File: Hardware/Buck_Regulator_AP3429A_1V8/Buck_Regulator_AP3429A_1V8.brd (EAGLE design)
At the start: 25.4 x 25.4 mm, 51 parts, among them J1 Screw Terminal, J2 POWER_JACKPOWER_JACK_SLOT_COM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, J3 Breakout Headers, U1 AP3429/A

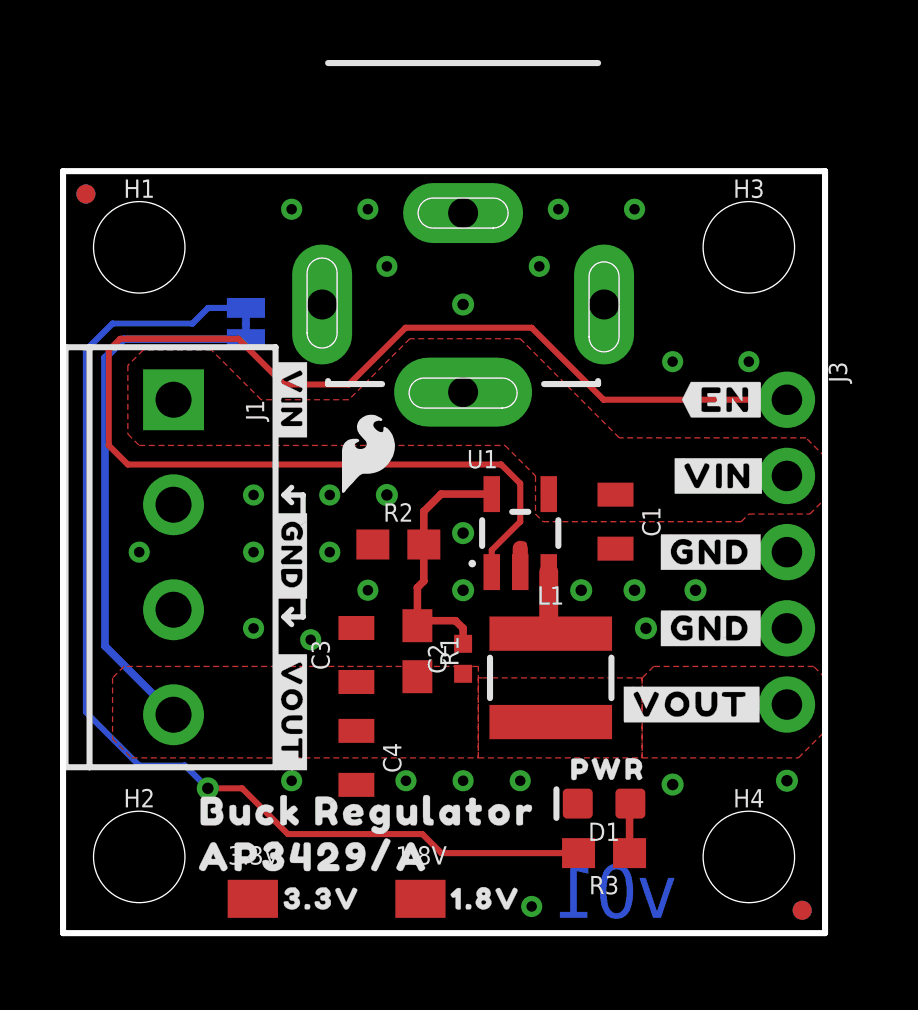
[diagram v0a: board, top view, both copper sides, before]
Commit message: Nudge traces for better GND pour connection on BRD
Moved some traces for a better GND pour on the top layer.
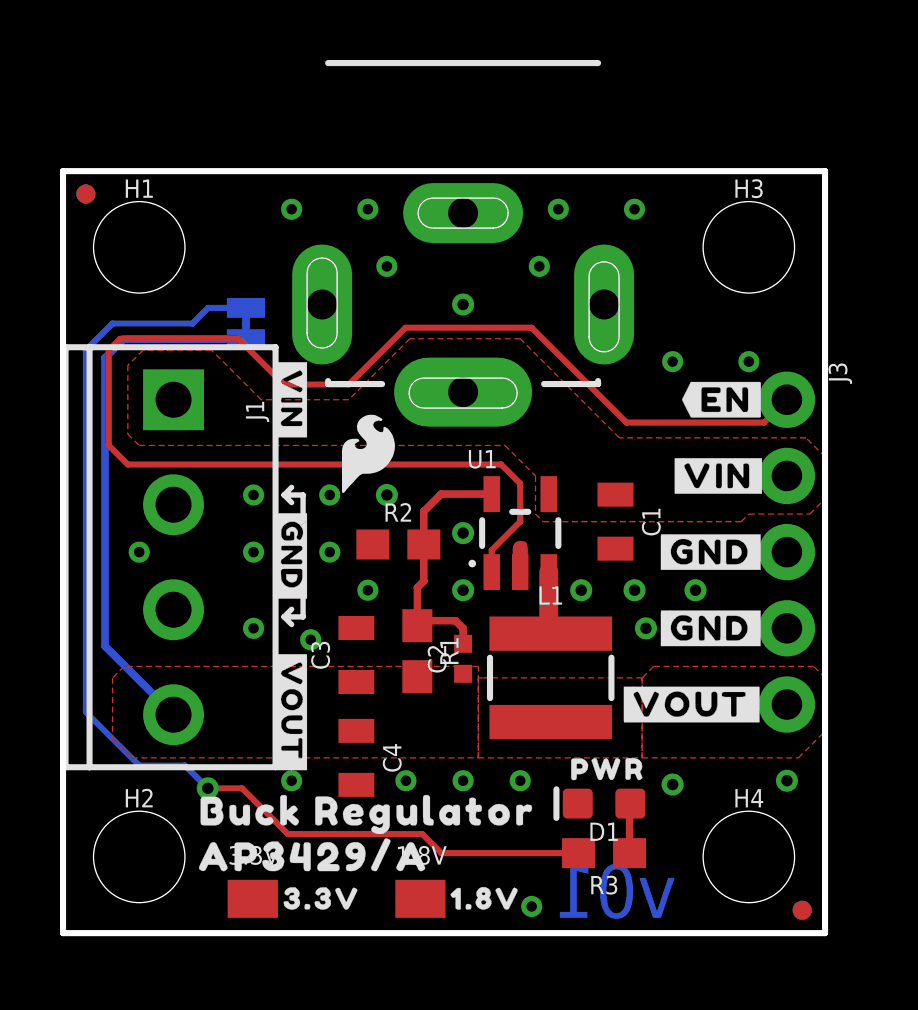
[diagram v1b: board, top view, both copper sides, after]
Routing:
- net EN: track 45.9 -> 46.6 mm
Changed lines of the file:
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@@
 <wire x1="1.524" y1="16.256" x2="1.524" y2="19.431" width="0.2032" layer="1"/>
 <wire x1="1.524" y1="19.431" x2="1.905" y2="19.812" width="0.2032" layer="1"/>
-<wire x1="15.61835" y1="20.1803" x2="18.01865" y2="17.78" width="0.2032" layer="1"/>
+<wire x1="15.61835" y1="20.1803" x2="18.78065" y2="17.018" width="0.2032" layer="1"/>
 <wire x1="1.905" y1="19.812" x2="5.842" y2="19.812" width="0.2032" layer="1"/>
 <wire x1="5.842" y1="19.812" x2="7.366" y2="18.288" width="0.2032" layer="1"/>
@@
 <wire x1="9.525" y1="18.288" x2="11.4173" y2="20.1803" width="0.2032" layer="1"/>
 <wire x1="11.4173" y1="20.1803" x2="15.61835" y2="20.1803" width="0.2032" layer="1"/>
-<wire x1="24.13" y1="17.78" x2="18.01865" y2="17.78" width="0.2032" layer="1"/>
+<wire x1="24.13" y1="17.78" x2="23.368" y2="17.018" width="0.2032" layer="1"/>
+<wire x1="23.368" y1="17.018" x2="18.78065" y2="17.018" width="0.2032" layer="1"/>
 </signal>
 <signal name="N$3">

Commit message: Added correct measurements
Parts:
- moved FRAME1 24.1 mm to (-10.2, -41.9)
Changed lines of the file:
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@@
 <drawing>
 <settings>
-<setting alwaysvectorfont="yes"/>
+<setting alwaysvectorfont="no"/>
 <setting verticaltext="up"/>
 </settings>
@@
 <layer number="45" name="Holes" color="7" fill="1" visible="yes" active="yes"/>
 <layer number="46" name="Milling" color="3" fill="1" visible="no" active="yes"/>
-<layer number="47" name="Measures" color="7" fill="1" visible="no" active="yes"/>
+<layer number="47" name="Measures" color="7" fill="1" visible="yes" active="yes"/>
 <layer number="48" name="Document" color="7" fill="1" visible="no" active="yes"/>
 <layer number="49" name="Reference" color="7" fill="1" visible="no" active="yes"/>
@@
 <wire x1="7.366" y1="10.541" x2="7.62" y2="10.287" width="0.1778" layer="21"/>
 <text x="20.447" y="0.508" size="1.778" layer="16" font="vector" ratio="15" rot="MR0">v01</text>
-<text x="16.51" y="-17.78" size="1.778" layer="51" font="vector" ratio="10" distance="15">M. Chodikov</text>
-<text x="5.08" y="46.99" size="1.778" layer="47" font="vector" ratio="15">Units in Inches</text>
+<text x="16.51" y="-41.91" size="1.778" layer="51" font="vector" ratio="10" distance="15">M. Chodikov</text>
 <wire x1="5.334" y1="11.176" x2="5.334" y2="10.414" width="0.2032" layer="22"/>
 <wire x1="5.334" y1="10.414" x2="4.826" y2="10.414" width="0.2032" layer="22"/>
@@
 <rectangle x1="6.35" y1="3.81" x2="21.59" y2="16.51" layer="30" rot="R180"/>
 <wire x1="5.08" y1="11.43" x2="5.334" y2="11.176" width="0.2032" layer="22"/>
-<dimension x1="25.4" y1="25.4" x2="22.86" y2="25.4" x3="24.13" y3="29.21" textsize="1.778" textratio="15" layer="47" unit="inch"/>
-<dimension x1="2.54" y1="22.86" x2="0" y2="22.86" x3="1.27" y3="35.56" textsize="1.778" textratio="15" layer="47" unit="inch"/>
-<dimension x1="25.4" y1="25.4" x2="0" y2="25.4" x3="12.7" y3="40.64" textsize="1.778" textratio="15" layer="47" unit="inch"/>
-<dimension x1="2.54" y1="2.54" x2="2.54" y2="0" x3="-2.54" y3="1.27" textsize="1.778" textratio="15" layer="47" unit="inch"/>
-<dimension x1="2.54" y1="22.86" x2="2.54" y2="25.4" x3="-2.54" y3="24.13" textsize="1.778" textratio="15" layer="47" unit="inch"/>
-<dimension x1="3.683" y1="7.28" x2="3.81" y2="0" x3="-8.89" y3="3.64" textsize="1.778" textratio="15" layer="47" dtype="vertical" unit="inch"/>
-<dimension x1="3.683" y1="7.28" x2="3.81" y2="10.795" x3="-13.97" y3="9.0375" textsize="1.778" textratio="15" layer="47" dtype="vertical" unit="inch"/>
-<dimension x1="0" y1="25.4" x2="0" y2="0" x3="-20.32" y3="12.7" textsize="1.778" textratio="15" layer="47" unit="inch"/>
-<dimension x1="24.13" y1="7.493" x2="24.13" y2="0" x3="30.48" y3="3.7465" textsize="1.778" textratio="15" layer="47" unit="inch"/>
-<dimension x1="24.13" y1="7.62" x2="24.13" y2="10.16" x3="30.48" y3="8.89" textsize="1.778" textratio="15" layer="47" unit="inch"/>
+<dimension x1="2.54" y1="2.54" x2="0" y2="2.54" x3="1.27" y3="-3.81" textsize="1.778" layer="47" unit="inch"/>
+<dimension x1="3.683" y1="7.28" x2="3.683" y2="0" x3="-3.81" y3="3.64" textsize="1.778" layer="47" dtype="vertical" unit="inch"/>
+<dimension x1="24.13" y1="7.62" x2="24.13" y2="0" x3="-7.62" y3="3.81" textsize="1.778" layer="47" dtype="vertical" unit="inch"/>
+<dimension x1="24.13" y1="10.16" x2="24.13" y2="0" x3="-12.7" y3="5.08" textsize="1.778" layer="47" dtype="vertical" unit="inch"/>
+<dimension x1="3.683" y1="10.795" x2="3.937" y2="0" x3="-17.78" y3="5.3975" textsize="1.778" layer="47" dtype="vertical" unit="inch"/>
+<text x="-22.86" y="-10.16" size="1.778" layer="47" font="vector" ratio="15">Units in Inches</text>
+<dimension x1="2.54" y1="2.54" x2="2.54" y2="0" x3="-21.59" y3="1.27" textsize="1.778" layer="47" dtype="vertical" unit="inch"/>
+<dimension x1="2.54" y1="22.86" x2="2.54" y2="0" x3="-25.4" y3="11.43" textsize="1.778" layer="47" dtype="vertical" unit="inch"/>
+<dimension x1="13.335" y1="24.003" x2="13.97" y2="0" x3="-29.21" y3="12.0015" textsize="1.778" layer="47" dtype="vertical" unit="inch"/>
+<dimension x1="0" y1="0" x2="2.54" y2="25.4" x3="-33.02" y3="12.7" textsize="1.778" layer="47" dtype="vertical" unit="inch"/>
+<dimension x1="3.683" y1="17.78" x2="0" y2="17.78" x3="1.8415" y3="-7.62" textsize="1.778" layer="47" dtype="vertical" unit="inch"/>
+<dimension x1="13.335" y1="24.003" x2="0" y2="24.003" x3="6.6675" y3="-12.7" textsize="1.778" layer="47" dtype="vertical" unit="inch"/>
+<dimension x1="22.86" y1="2.54" x2="0" y2="2.54" x3="11.43" y3="-17.78" textsize="1.778" layer="47" dtype="vertical" unit="inch"/>
+<dimension x1="24.13" y1="7.62" x2="0" y2="7.62" x3="12.065" y3="-22.86" textsize="1.778" layer="47" dtype="vertical" unit="inch"/>
+<dimension x1="25.4" y1="0" x2="0" y2="0" x3="12.7" y3="-27.94" textsize="1.778" layer="47" dtype="vertical" unit="inch"/>
 </plain>
 <attributes>
@@
 <element name="FD3" library="SparkFun-Aesthetics" package="FIDUCIAL-MICRO" value="FIDUCIALUFIDUCIAL" x="0.762" y="24.638" smashed="yes" rot="MR0"/>
 <element name="FD4" library="SparkFun-Aesthetics" package="FIDUCIAL-MICRO" value="FIDUCIALUFIDUCIAL" x="0.762" y="24.638" smashed="yes"/>
-<element name="FRAME1" library="SparkFun-Aesthetics" package="CREATIVE_COMMONS" value="FRAME-LEDGER" x="-10.16" y="-17.78" smashed="yes">
-<attribute name="DESIGNER" value="M. Chodikov" x="69.85" y="-30.48" size="1.778" layer="27" display="off"/>
-<attribute name="REV" value="v01" x="69.85" y="-30.48" size="1.778" layer="27" display="off"/>
+<element name="FRAME1" library="SparkFun-Aesthetics" package="CREATIVE_COMMONS" value="FRAME-LEDGER" x="-10.16" y="-41.91" smashed="yes">
+<attribute name="DESIGNER" value="M. Chodikov" x="69.85" y="-54.61" size="1.778" layer="27" display="off"/>
+<attribute name="REV" value="v01" x="69.85" y="-54.61" size="1.778" layer="27" display="off"/>
 </element>
 <element name="L1" library="SparkFun-Coils" package="INDUCTOR_4X4MM" value="2.2μH" x="16.256" y="8.509" smashed="yes">

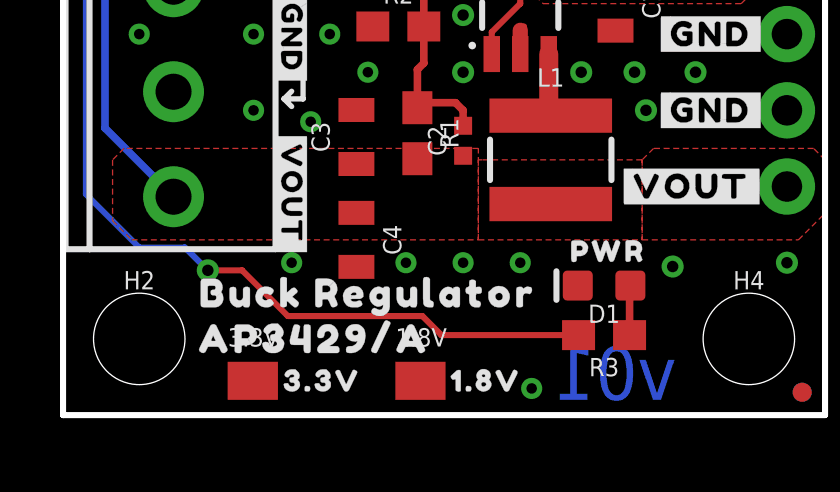
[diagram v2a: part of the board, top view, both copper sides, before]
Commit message: Further design review changes - v01
Added selective solder path to Document layer for the terminal block; moved the silkscreen name on the front to not be covered by the mounting hole anymore when a user uses a screw; nudges the LED power trace over for better GND connection; added measures to thermal pad (in reference to bottom right, and for the size)
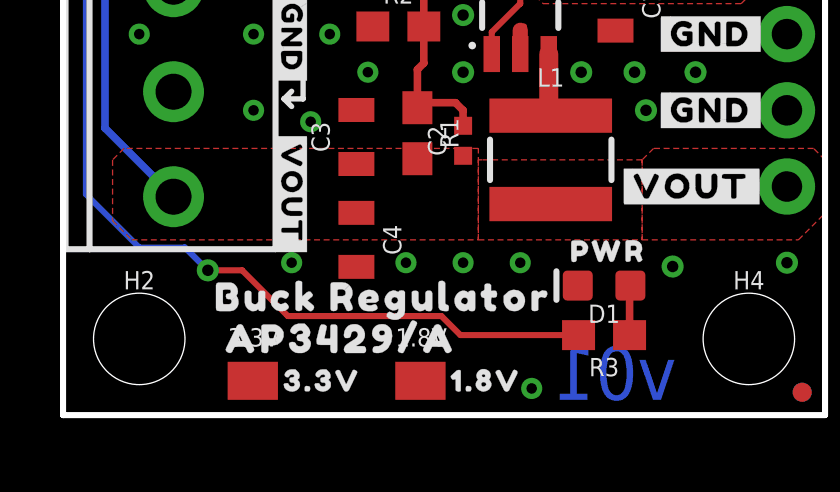
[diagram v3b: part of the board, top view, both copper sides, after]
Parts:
- moved FRAME1 2.54 mm to (-10.2, -44.5)
- moved U$3 0.89 mm to (9.27, 2.54)
- moved U$2 0.52 mm to (10.7, 3.94)
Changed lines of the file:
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@@
 <layer number="28" name="bValues" color="7" fill="1" visible="no" active="yes"/>
 <layer number="29" name="tStop" color="7" fill="3" visible="no" active="yes"/>
-<layer number="30" name="bStop" color="7" fill="6" visible="no" active="yes"/>
+<layer number="30" name="bStop" color="7" fill="6" visible="yes" active="yes"/>
 <layer number="31" name="tCream" color="7" fill="4" visible="no" active="yes"/>
 <layer number="32" name="bCream" color="7" fill="5" visible="no" active="yes"/>
@@
 <wire x1="7.366" y1="10.541" x2="7.62" y2="10.287" width="0.1778" layer="21"/>
 <text x="20.447" y="0.508" size="1.778" layer="16" font="vector" ratio="15" rot="MR0">v01</text>
-<text x="16.51" y="-41.91" size="1.778" layer="51" font="vector" ratio="10" distance="15">M. Chodikov</text>
+<text x="16.51" y="-44.45" size="1.778" layer="51" font="vector" ratio="10" distance="15">M. Chodikov</text>
 <wire x1="5.334" y1="11.176" x2="5.334" y2="10.414" width="0.2032" layer="22"/>
 <wire x1="5.334" y1="10.414" x2="4.826" y2="10.414" width="0.2032" layer="22"/>
@@
 <dimension x1="3.683" y1="10.795" x2="3.937" y2="0" x3="-17.78" y3="5.3975" textsize="1.778" layer="47" dtype="vertical" unit="inch"/>
 <text x="-22.86" y="-10.16" size="1.778" layer="47" font="vector" ratio="15">Units in Inches</text>
-<dimension x1="2.54" y1="2.54" x2="2.54" y2="0" x3="-21.59" y3="1.27" textsize="1.778" layer="47" dtype="vertical" unit="inch"/>
-<dimension x1="2.54" y1="22.86" x2="2.54" y2="0" x3="-25.4" y3="11.43" textsize="1.778" layer="47" dtype="vertical" unit="inch"/>
-<dimension x1="13.335" y1="24.003" x2="13.97" y2="0" x3="-29.21" y3="12.0015" textsize="1.778" layer="47" dtype="vertical" unit="inch"/>
-<dimension x1="0" y1="0" x2="2.54" y2="25.4" x3="-33.02" y3="12.7" textsize="1.778" layer="47" dtype="vertical" unit="inch"/>
 <dimension x1="3.683" y1="17.78" x2="0" y2="17.78" x3="1.8415" y3="-7.62" textsize="1.778" layer="47" dtype="vertical" unit="inch"/>
-<dimension x1="13.335" y1="24.003" x2="0" y2="24.003" x3="6.6675" y3="-12.7" textsize="1.778" layer="47" dtype="vertical" unit="inch"/>
-<dimension x1="22.86" y1="2.54" x2="0" y2="2.54" x3="11.43" y3="-17.78" textsize="1.778" layer="47" dtype="vertical" unit="inch"/>
-<dimension x1="24.13" y1="7.62" x2="0" y2="7.62" x3="12.065" y3="-22.86" textsize="1.778" layer="47" dtype="vertical" unit="inch"/>
-<dimension x1="25.4" y1="0" x2="0" y2="0" x3="12.7" y3="-27.94" textsize="1.778" layer="47" dtype="vertical" unit="inch"/>
+<wire x1="3.048" y1="16.891" x2="3.048" y2="6.35" width="5.9944" layer="48"/>
+<wire x1="3.048" y1="6.35" x2="0" y2="3.302" width="5.9944" layer="48"/>
+<dimension x1="6.35" y1="3.81" x2="0" y2="3.81" x3="3.175" y3="-12.7" textsize="1.778" textratio="15" layer="47" unit="inch"/>
+<dimension x1="13.335" y1="24.003" x2="0" y2="24.003" x3="6.6675" y3="-19.05" textsize="1.778" textratio="15" layer="47" unit="inch"/>
+<dimension x1="22.86" y1="2.54" x2="0" y2="2.54" x3="11.43" y3="-24.13" textsize="1.778" textratio="15" layer="47" unit="inch"/>
+<dimension x1="24.13" y1="7.62" x2="0" y2="7.62" x3="12.065" y3="-29.21" textsize="1.778" textratio="15" layer="47" unit="inch"/>
+<dimension x1="25.4" y1="0" x2="0" y2="0" x3="12.7" y3="-33.02" textsize="1.778" textratio="15" layer="47" unit="inch"/>
+<dimension x1="6.35" y1="3.81" x2="6.35" y2="0" x3="-21.59" y3="1.905" textsize="1.778" textratio="15" layer="47" unit="inch"/>
+<dimension x1="2.54" y1="2.54" x2="2.54" y2="0" x3="-25.4" y3="1.27" textsize="1.778" textratio="15" layer="47" unit="inch"/>
+<dimension x1="2.54" y1="22.86" x2="2.54" y2="0" x3="-29.21" y3="11.43" textsize="1.778" textratio="15" layer="47" unit="inch"/>
+<dimension x1="13.335" y1="24.003" x2="13.335" y2="0" x3="-33.02" y3="12.0015" textsize="1.778" textratio="15" layer="47" unit="inch"/>
+<dimension x1="0" y1="0" x2="0" y2="25.4" x3="-36.83" y3="12.7" textsize="1.778" textratio="15" layer="47" unit="inch"/>
+<dimension x1="6.35" y1="3.81" x2="21.59" y2="3.81" x3="13.97" y3="34.29" textsize="1.778" textratio="15" layer="47" unit="inch"/>
+<dimension x1="21.59" y1="3.81" x2="21.59" y2="16.51" x3="30.48" y3="10.16" textsize="1.778" textratio="15" layer="47" unit="inch"/>
 </plain>
 <attributes>
@@
 <element name="FD3" library="SparkFun-Aesthetics" package="FIDUCIAL-MICRO" value="FIDUCIALUFIDUCIAL" x="0.762" y="24.638" smashed="yes" rot="MR0"/>
 <element name="FD4" library="SparkFun-Aesthetics" package="FIDUCIAL-MICRO" value="FIDUCIALUFIDUCIAL" x="0.762" y="24.638" smashed="yes"/>
-<element name="FRAME1" library="SparkFun-Aesthetics" package="CREATIVE_COMMONS" value="FRAME-LEDGER" x="-10.16" y="-41.91" smashed="yes">
-<attribute name="DESIGNER" value="M. Chodikov" x="69.85" y="-54.61" size="1.778" layer="27" display="off"/>
-<attribute name="REV" value="v01" x="69.85" y="-54.61" size="1.778" layer="27" display="off"/>
+<element name="FRAME1" library="SparkFun-Aesthetics" package="CREATIVE_COMMONS" value="FRAME-LEDGER" x="-10.16" y="-44.45" smashed="yes">
+<attribute name="DESIGNER" value="M. Chodikov" x="69.85" y="-57.15" size="1.778" layer="27" display="off"/>
+<attribute name="REV" value="v01" x="69.85" y="-57.15" size="1.778" layer="27" display="off"/>
 </element>
 <element name="L1" library="SparkFun-Coils" package="INDUCTOR_4X4MM" value="2.2μH" x="16.256" y="8.509" smashed="yes">
@@
 <attribute name="VALUE" x="22.098" y="19.05" size="0.6096" layer="27" font="vector" ratio="20" rot="R270"/>
 </element>
-<element name="U$2" library="output" package="BUCK_REGULATOR24" value="" x="10.16" y="4.064" smashed="yes"/>
-<element name="U$3" library="output" package="AP3429#A25" value="" x="8.382" y="2.54" smashed="yes"/>
+<element name="U$2" library="output" package="BUCK_REGULATOR24" value="" x="10.668" y="3.937" smashed="yes"/>
+<element name="U$3" library="output" package="AP3429#A25" value="" x="9.271" y="2.54" smashed="yes"/>
 <element name="U$4" library="output" package="#VOUT#3431" value="" x="20.955" y="7.62" smashed="yes"/>
 <element name="U$5" library="output" package="#GND#3432" value="" x="21.59" y="10.16" smashed="yes"/>
@@
 <wire x1="4.8387" y1="20.8407" x2="4.318" y2="20.32" width="0.2032" layer="16"/>
 <wire x1="4.318" y1="20.32" x2="1.651" y2="20.32" width="0.2032" layer="16"/>
-<wire x1="12.612" y1="2.667" x2="17.184" y2="2.667" width="0.2032" layer="1"/>
-<wire x1="12.612" y1="2.667" x2="11.977" y2="3.302" width="0.2032" layer="1"/>
-<wire x1="11.977" y1="3.302" x2="7.493" y2="3.302" width="0.2032" layer="1"/>
+<wire x1="13.247" y1="2.667" x2="17.184" y2="2.667" width="0.2032" layer="1"/>
+<wire x1="13.247" y1="2.667" x2="12.612" y2="3.302" width="0.2032" layer="1"/>
+<wire x1="12.612" y1="3.302" x2="7.493" y2="3.302" width="0.2032" layer="1"/>
 <via x="4.826" y="4.826" extent="1-16" drill="0.381"/>
 <wire x1="4.826" y1="4.826" x2="5.969" y2="4.826" width="0.2032" layer="1"/>
